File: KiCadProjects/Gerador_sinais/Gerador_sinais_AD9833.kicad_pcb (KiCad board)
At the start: 2 copper layers, 90 x 100 mm, 9 parts, among them J1 tensoes, J2 Conn_01x05, J5 sinais, J6 comunicacao, U1 AD828AN

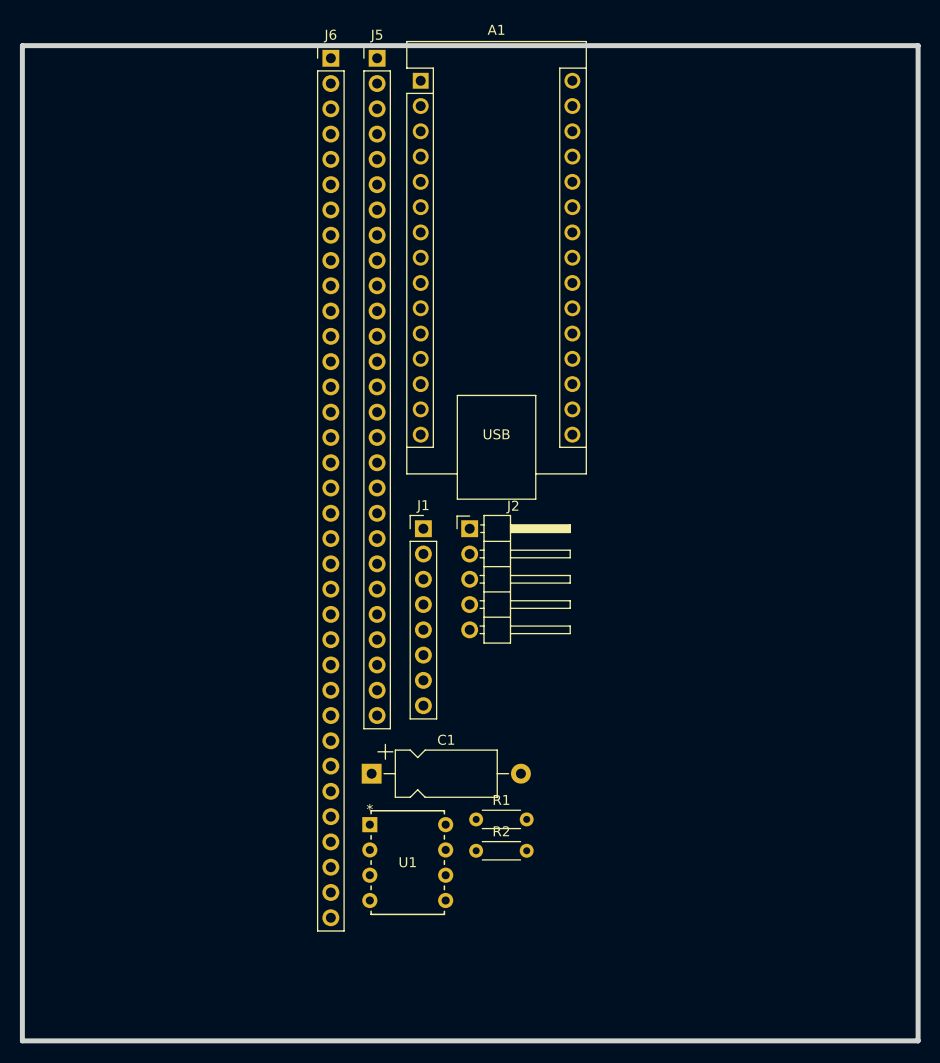
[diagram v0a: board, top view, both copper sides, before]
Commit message: Conexão do arduino nano ao I2c 1
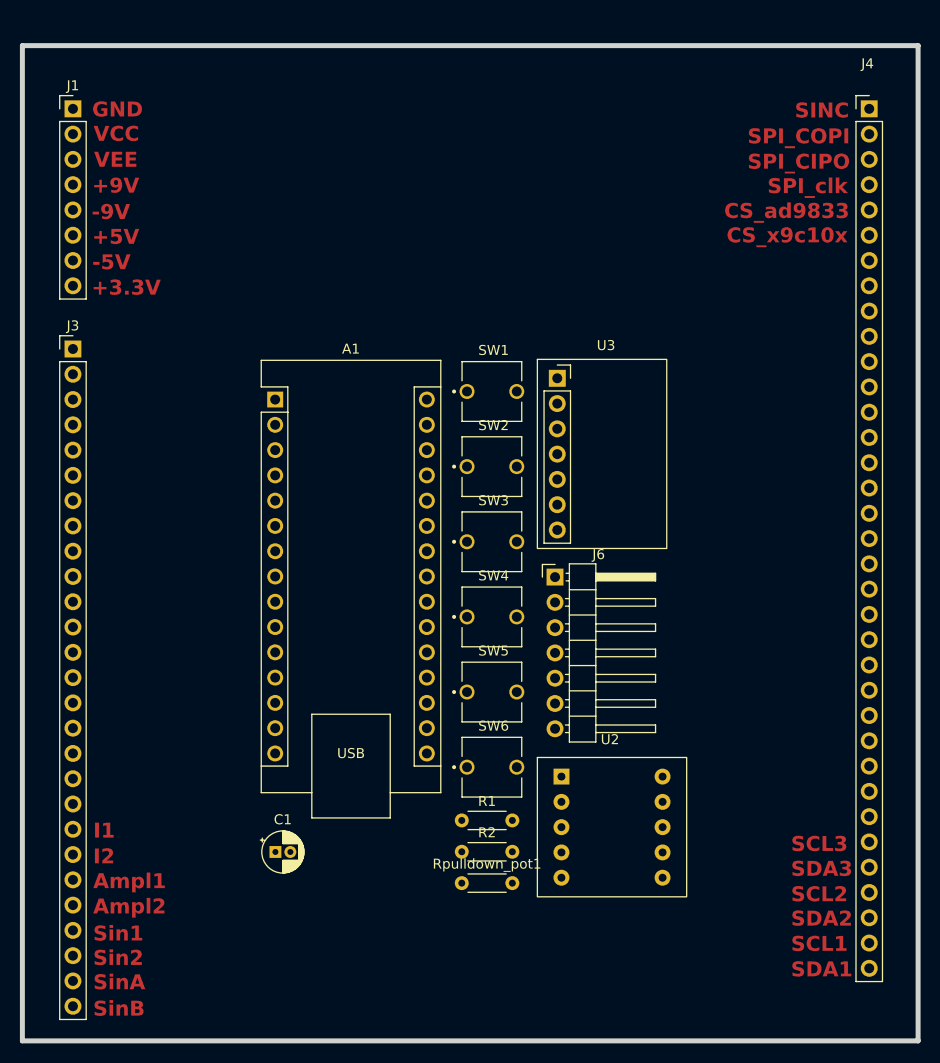
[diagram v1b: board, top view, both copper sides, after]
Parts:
- removed J2: Conn_01x05, Connector_PinHeader_2.54mm:PinHeader_1x05_P2.54mm_Horizontal
- removed J5: sinais, Connector_PinHeader_2.54mm:PinHeader_1x27_P2.54mm_Vertical
- removed U1: AD828AN, footprints:N_8_ADI
- added J3: sinais analogicos, Connector_PinHeader_2.54mm:PinHeader_1x27_P2.54mm_Vertical, F.Cu at (106.7, 81.3)
- added J4: comunicacao / sinais digitais, Connector_PinHeader_2.54mm:PinHeader_1x35_P2.54mm_Vertical, F.Cu at (186.7, 57.1)
- added Rpulldown_pot1: 10k, Resistor_THT:R_Axial_DIN0204_L3.6mm_D1.6mm_P5.08mm_Horizontal, F.Cu at (145.8, 134.9)
- added SW1: botao_forma_onda, push_button_2_pin:SW_BUTT-2, F.Cu at (148.8, 85.5)
- added SW2: botao_incremento_freq, push_button_2_pin:SW_BUTT-2, F.Cu at (148.8, 93.1)
- added SW3: botao_decremento_freq, push_button_2_pin:SW_BUTT-2, F.Cu at (148.8, 100.7)
- added SW4: botao_save_Rgain, push_button_2_pin:SW_BUTT-2, F.Cu at (148.8, 108.2)
- added SW5: botao_aumenta_Rgain, push_button_2_pin:SW_BUTT-2, F.Cu at (148.8, 115.8)
- added SW6: botao_diminui_Rgain, push_button_2_pin:SW_BUTT-2, F.Cu at (148.8, 123.3)
- added U2: X9c10x, X9c10X_module:X9c10X_module, F.Cu at (160.8, 129.3)
- added U3: AD9833_module, AD9833_module:AD9833_module, F.Cu at (155.3, 84.2)
- C1: footprint Capacitor_THT:CP_Axial_L10.0mm_D4.5mm_P15.00mm_Horizontal -> Capacitor_THT:CP_Radial_D4.0mm_P1.50mm
- J6: value comunicacao -> pinos de prova; footprint Connector_PinHeader_2.54mm:PinHeader_1x35_P2.54mm_Vertical -> Connector_PinHeader_2.54mm:PinHeader_1x07_P2.54mm_Horizontal
- R2: value R -> 2,7k
- moved J6 56.8 mm to (155.1, 104.2)
- moved J1 55.0 mm to (106.7, 57.1)
- moved A1 35.2 mm to (127.0, 86.4)
- moved C1 12.5 mm to (127.0, 131.8)
- moved R1 1.45 mm to (145.8, 128.7)
- moved R2 1.45 mm to (145.8, 131.8)
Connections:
- A1 pad 10: unconnected-(A1-D7-Pad10) -> X9c10x_INC
- A1 pad 11: unconnected-(A1-D8-Pad11) -> X9c10x_U/D
- A1 pad 12: unconnected-(A1-D9-Pad12) -> freq+
- A1 pad 13: unconnected-(A1-D10-Pad13) -> freq-
- A1 pad 14: unconnected-(A1-D11-Pad14) -> SPI_COPI
- A1 pad 15: unconnected-(A1-D12-Pad15) -> S_wave
- A1 pad 16: unconnected-(A1-D13-Pad16) -> SPI_clk
- A1 pad 5: unconnected-(A1-D2-Pad5) -> CS (X9c104)
- A1 pad 7: unconnected-(A1-D4-Pad7) -> CS (AD9833)
- A1 pad 8: unconnected-(A1-D5-Pad8) -> Up_pot
- A1 pad 9: unconnected-(A1-D6-Pad9) -> Down_pot
- C1 pad 1: Net-(U3-OUT) -> Out_ad9833
- C1 pad 2: Net-(C1-Pad2) -> Passa_alta
- J6 pad 1: unconnected-(J6-Pin_1-Pad1) -> Earth
- J6 pad 2: unconnected-(J6-Pin_2-Pad2) -> +5V
- J6 pad 3: unconnected-(J6-Pin_3-Pad3) -> -9V
- J6 pad 4: unconnected-(J6-Pin_4-Pad4) -> +9V
- J6 pad 5: unconnected-(J6-Pin_5-Pad5) -> Out_ad9833
- J6 pad 6: unconnected-(J6-Pin_6-Pad6) -> Passa_alta
- J6 pad 7: unconnected-(J6-Pin_7-Pad7) -> Out_circuito
- R1 pad 1: Net-(C1-Pad2) -> Passa_alta
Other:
- board text added: "+3.3V"
- board text added: "+5V"
- board text added: "+9V"
- board text added: "-5V"
- board text added: "-9V"
- board text added: "Ampl1"
- board text added: "Ampl2"
- board text added: "CS_ad9833"
- board text added: "CS_x9c10x"
- board text added: "GND"
- board text added: "I1"
- board text added: "I2"
- board text added: "SCL1"
- board text added: "SCL2"
- board text added: "SCL3"
- board text added: "SDA1"
- board text added: "SDA2"
- board text added: "SDA3"
- board text added: "SINC"
- board text added: "SPI_CIPO"
- board text added: "SPI_COPI"
- board text added: "SPI_clk"
- board text added: "Sin1"
- board text added: "Sin2"
- board text added: "SinA"
- board text added: "SinB"
- board text added: "VCC"
- board text added: "VEE"

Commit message: Esquema PCB
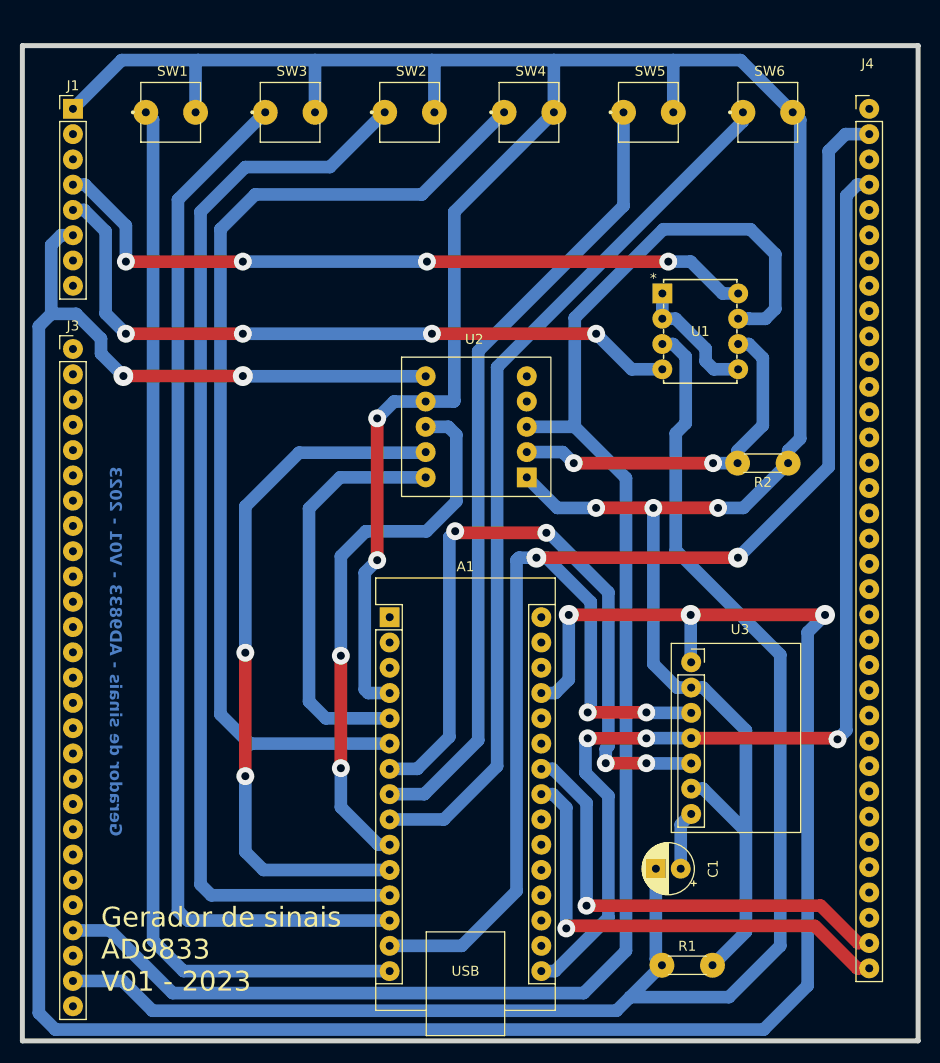
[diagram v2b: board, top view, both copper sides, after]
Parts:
- removed J6: pinos de prova, Connector_PinHeader_2.54mm:PinHeader_1x07_P2.54mm_Horizontal
- removed Rpulldown_pot1: 10k, Resistor_THT:R_Axial_DIN0204_L3.6mm_D1.6mm_P5.08mm_Horizontal
- added U1: AD828AN, AD828:N_8_ADI, F.Cu at (165.9, 75.7)
- C1: footprint Capacitor_THT:CP_Radial_D4.0mm_P1.50mm -> Capacitor_THT:CP_Radial_D5.0mm_P2.50mm
- moved SW6 71.4 mm to (176.5, 57.5)
- moved SW5 60.3 mm to (164.5, 57.5)
- moved R2 51.0 mm to (178.5, 92.8), turned to 180 degrees
- moved SW4 50.8 mm to (152.5, 57.5)
- moved SW3 47.7 mm to (128.5, 57.5)
- moved SW1 42.8 mm to (116.5, 57.5)
- moved U2 42.5 mm to (147.2, 89.1)
- moved C1 40.8 mm to (167.8, 133.5), turned to 180 degrees
- moved SW2 36.5 mm to (140.5, 57.5)
- moved U3 31.5 mm to (168.8, 112.8)
- moved R1 24.8 mm to (165.9, 143.2)
- moved A1 24.7 mm to (138.5, 108.2)
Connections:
- A1 pad 17: +3.3V -> unconnected-(A1-3V3-Pad17)
- A1 pad 23: unconnected-(A1-A4-Pad23) -> SDA1
- A1 pad 24: unconnected-(A1-A5-Pad24) -> SCL1
- A1 pad 29: Earth -> unconnected-(A1-GND-Pad29)
- A1 pad 6: unconnected-(A1-D3-Pad6) -> storage_R
- SW4 pad 1: +5V -> storage_R
- SW4 pad 2: CS (X9c104) -> Earth
- U2 pad 10: +5V -> unconnected-(U2-VCC-Pad10)
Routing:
- net Earth: track 0.00 -> 300.5 mm, vias 0 -> 5
- net +5V: track 0.00 -> 279.5 mm, vias 0 -> 5
- net Out_circuito: track 0.00 -> 165.0 mm
- net Passa_alta: track 0.00 -> 156.3 mm
- net SPI_COPI: track 0.00 -> 149.0 mm, vias 0 -> 4
- net SPI_clk: track 0.00 -> 111.7 mm, vias 0 -> 3
- net freq+: track 0.00 -> 109.7 mm
- net S_wave: track 0.00 -> 108.6 mm
- net freq-: track 0.00 -> 105.5 mm
- net storage_R: track 0.00 -> 100.4 mm
- net Down_pot: track 0.00 -> 88.9 mm
- net Up_pot: track 0.00 -> 80.3 mm
- net +9V: track 0.00 -> 73.5 mm, vias 0 -> 4
- net CS (AD9833): track 0.00 -> 72.0 mm, vias 0 -> 4
- net -9V: track 0.00 -> 70.7 mm, vias 0 -> 4
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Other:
- board text added: "Gerador de sinais - AD9833 - V01 - 2023"
- board text added: "Gerador de sinais AD9833 V01 - 2023"
- board text removed: "+3.3V"
- board text removed: "+5V"
- board text removed: "+9V"
- board text removed: "-5V"
- board text removed: "-9V"
- board text removed: "Ampl1"
- board text removed: "Ampl2"
- board text removed: "CS_ad9833"
- board text removed: "CS_x9c10x"
- board text removed: "GND"
- board text removed: "I1"
- board text removed: "I2"
- board text removed: "SCL1"
- board text removed: "SCL2"
- board text removed: "SCL3"
- board text removed: "SDA1"
- board text removed: "SDA2"
- board text removed: "SDA3"
- board text removed: "SINC"
- board text removed: "SPI_CIPO"
- board text removed: "SPI_COPI"
- board text removed: "SPI_clk"
- board text removed: "Sin1"
- board text removed: "Sin2"
- board text removed: "SinA"
- board text removed: "SinB"
- board text removed: "VCC"
- board text removed: "VEE"

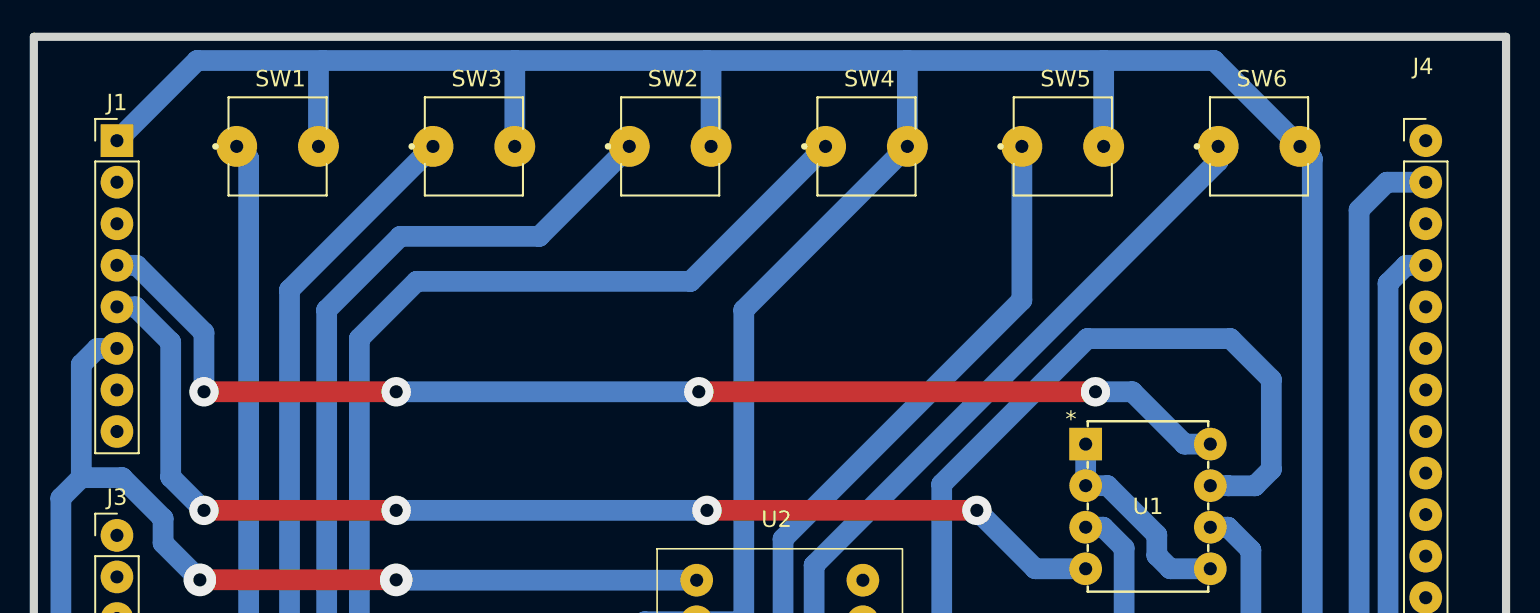
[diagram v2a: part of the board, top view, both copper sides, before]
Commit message: Esquema PCB
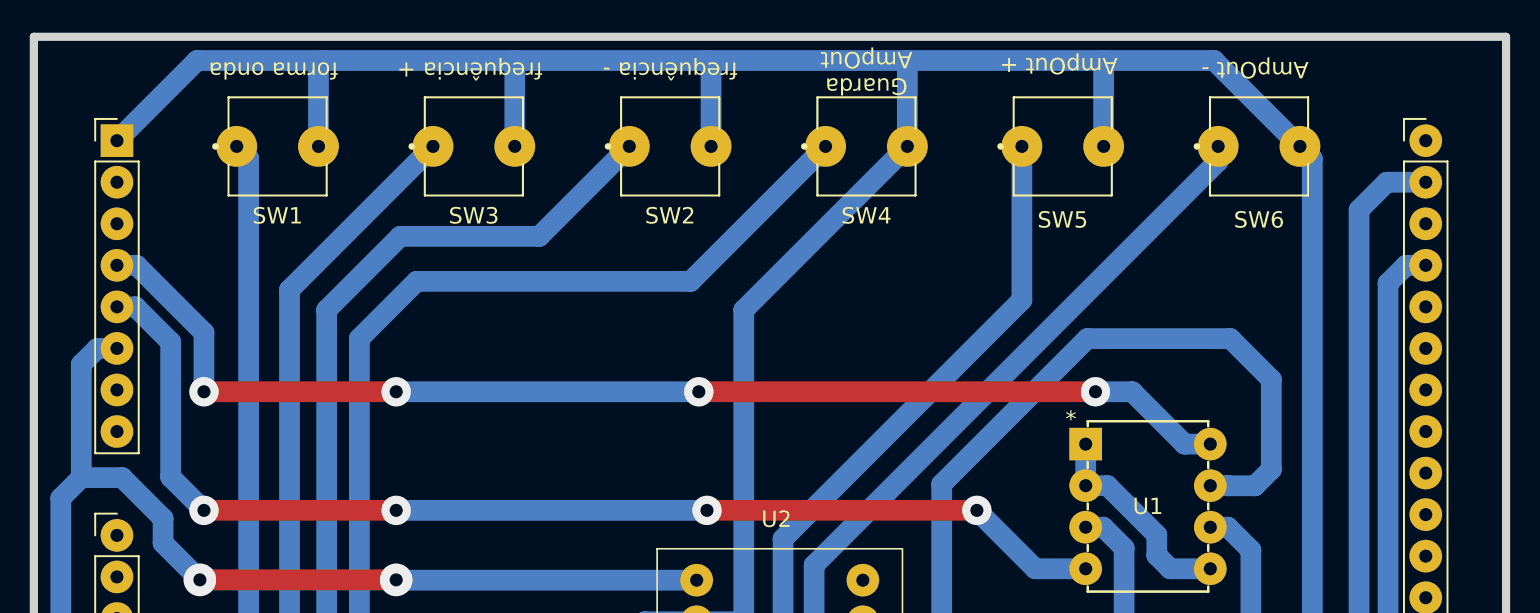
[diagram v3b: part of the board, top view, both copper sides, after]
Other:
- board text added: "AmpOut +"
- board text added: "AmpOut -"
- board text added: "Guarda AmpOut"
- board text added: "forma onda"
- board text added: "frequência +"
- board text added: "frequência -"
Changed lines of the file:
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@@
     (property "ki_keywords" "switch normally-open pushbutton push-button")
     (attr through_hole)
-    (fp_text reference "SW3" (at 0.175 -4.135) (layer "F.SilkS")
-        (effects (font (size 1 1) (thickness 0.15)))
-    )
-    (fp_text value "botao_decremento_freq" (at 0 7) (layer "F.Fab")
+    (fp_text reference "SW3" (at 0 4.25) (layer "F.SilkS")
+        (effects (font (size 1 1) (thickness 0.15)))
+    )
+    (fp_text value "botao_decremento_freq" (at 0 7) (layer "F.Fab") hide
         (effects (font (size 1 1) (thickness 0.15)))
     )
@@
     (property "ki_keywords" "switch normally-open pushbutton push-button")
     (attr through_hole)
-    (fp_text reference "SW4" (at 0.175 -4.135) (layer "F.SilkS")
-        (effects (font (size 1 1) (thickness 0.15)))
-    )
-    (fp_text value "botao_save_Rgain" (at 0 6.75) (layer "F.Fab")
+    (fp_text reference "SW4" (at 0 4.25) (layer "F.SilkS")
+        (effects (font (size 1 1) (thickness 0.15)))
+    )
+    (fp_text value "botao_save_Rgain" (at 0 6.75) (layer "F.Fab") hide
         (effects (font (size 1 1) (thickness 0.15)))
     )
@@
     (property "ki_keywords" "connector")
     (attr through_hole)
-    (fp_text reference "J4" (at -0.165 -4.535) (layer "F.SilkS")
-        (effects (font (size 1 1) (thickness 0.15)))
-    )
-    (fp_text value "comunicacao / sinais digitais" (at 0 88.69) (layer "F.Fab") hide
-        (effects (font (size 1 1) (thickness 0.15)))
-    )
-    (fp_text user "comunicacao" (at 3.264 18.96 90) (layer "F.Fab")
+    (fp_text reference "J4" (at -0.165 -4.535) (layer "F.SilkS") hide
+        (effects (font (size 1 1) (thickness 0.15)))
+    )
+    (fp_text value "comunicacao / sinais digitais" (at 3.06 43.35 90) (layer "F.Fab")
+        (effects (font (size 1 1) (thickness 0.15)))
+    )
+    (fp_text user "comunicacao" (at 3.264 18.96 90) (layer "F.Fab") hide
         (effects (font (size 1 1) (thickness 0.15)))
     )
@@
     (property "ki_keywords" "switch normally-open pushbutton push-button")
     (attr through_hole)
-    (fp_text reference "SW6" (at 0.175 -4.135) (layer "F.SilkS")
-        (effects (font (size 1 1) (thickness 0.15)))
-    )
-    (fp_text value "botao_diminui_Rgain" (at 0 6.25) (layer "F.Fab")
+    (fp_text reference "SW6" (at 0 4.5) (layer "F.SilkS")
+        (effects (font (size 1 1) (thickness 0.15)))
+    )
+    (fp_text value "botao_diminui_Rgain" (at 0 6.25) (layer "F.Fab") hide
         (effects (font (size 1 1) (thickness 0.15)))
     )
@@
     (property "ki_keywords" "connector")
     (attr through_hole)
-    (fp_text reference "J1" (at 0 -2.33) (layer "F.SilkS")
+    (fp_text reference "J1" (at 0 -2.33) (layer "F.SilkS") hide
         (effects (font (size 1 1) (thickness 0.15)))
     )
@@
     (property "ki_keywords" "connector")
     (attr through_hole)
-    (fp_text reference "J3" (at 0 -2.33) (layer "F.SilkS")
+    (fp_text reference "J3" (at 0 -2.33) (layer "F.SilkS") hide
         (effects (font (size 1 1) (thickness 0.15)))
     )
@@
         (effects (font (size 1 1) (thickness 0.15)))
     )
-    (fp_text value "AD9833_module" (at 13.7 7.2 90) (layer "F.Fab")
+    (fp_text value "AD9833_module" (at 14.2 14.99 90) (layer "F.Fab")
         (effects (font (size 1 1) (thickness 0.15)))
     )
@@
     (property "ki_keywords" "switch normally-open pushbutton push-button")
     (attr through_hole)
-    (fp_text reference "SW2" (at 0.175 -4.135) (layer "F.SilkS")
-        (effects (font (size 1 1) (thickness 0.15)))
-    )
-    (fp_text value "botao_incremento_freq" (at 0 4.135) (layer "F.Fab")
+    (fp_text reference "SW2" (at 0 4.25) (layer "F.SilkS")
+        (effects (font (size 1 1) (thickness 0.15)))
+    )
+    (fp_text value "botao_incremento_freq" (at 0 4.135) (layer "F.Fab") hide
         (effects (font (size 1 1) (thickness 0.15)))
     )
@@
     (property "ki_keywords" "switch normally-open pushbutton push-button")
     (attr through_hole)
-    (fp_text reference "SW1" (at 0.175 -4.135) (layer "F.SilkS")
-        (effects (font (size 1 1) (thickness 0.15)))
-    )
-    (fp_text value "botao_forma_onda" (at 0 4.135) (layer "F.Fab")
+    (fp_text reference "SW1" (at 0 4.25) (layer "F.SilkS")
+        (effects (font (size 1 1) (thickness 0.15)))
+    )
+    (fp_text value "botao_forma_onda" (at -0.25 5.75) (layer "F.Fab") hide
         (effects (font (size 1 1) (thickness 0.15)))
     )
@@
     (property "ki_keywords" "switch normally-open pushbutton push-button")
     (attr through_hole)
-    (fp_text reference "SW5" (at 0.175 -4.135) (layer "F.SilkS")
-        (effects (font (size 1 1) (thickness 0.15)))
-    )
-    (fp_text value "botao_aumenta_Rgain" (at 0 4.135) (layer "F.Fab")
+    (fp_text reference "SW5" (at 0 4.5) (layer "F.SilkS")
+        (effects (font (size 1 1) (thickness 0.15)))
+    )
+    (fp_text value "botao_aumenta_Rgain" (at 0 4.135) (layer "F.Fab") hide
         (effects (font (size 1 1) (thickness 0.15)))
     )
@@
     (effects (font (size 1.2 1.2) (thickness 0.3) bold) (justify left bottom mirror))
   )
+  (gr_text "forma onda" (at 116.25 52.25 180) (layer "F.SilkS")
+    (effects (font (size 1 1) (thickness 0.15)) (justify bottom))
+  )
+  (gr_text "Guarda \nAmpOut\n\n" (at 152.5 50 180) (layer "F.SilkS")
+    (effects (font (size 1 1) (thickness 0.15)) (justify bottom))
+  )
+  (gr_text "frequência -\n" (at 140.5 52.25 180) (layer "F.SilkS")
+    (effects (font (size 1 1) (thickness 0.15)) (justify bottom))
+  )
+  (gr_text "AmpOut -\n\n\n" (at 176.25 49 180) (layer "F.SilkS")
+    (effects (font (size 1 1) (thickness 0.15)) (justify bottom))
+  )
+  (gr_text "AmpOut +\n\n\n" (at 164.25 48.75 180) (layer "F.SilkS")
+    (effects (font (size 1 1) (thickness 0.15)) (justify bottom))
+  )
+  (gr_text "frequência +\n" (at 128.25 52.25 180) (layer "F.SilkS")
+    (effects (font (size 1 1) (thickness 0.15)) (justify bottom))
+  )
   (gr_text "Gerador de sinais \nAD9833\nV01 - 2023\n" (at 109.5 146) (layer "F.SilkS")
